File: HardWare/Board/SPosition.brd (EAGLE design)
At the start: 60 x 110 mm, 64 parts

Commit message: board and schem revisions
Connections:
- net GND: now also U$1.AGND
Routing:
- net GND: track 538.3 -> 561.0 mm, vias 0 -> 1
- net +3V3: track 77.2 -> 78.8 mm
- net OLEDCLK: track 60.2 -> 60.8 mm
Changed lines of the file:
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@@
 <wire x1="1.0922" y1="81.2740875" x2="1.0922" y2="96.5" width="0.1524" layer="16"/>
 <wire x1="2.9277" y1="58.0049875" x2="1.0922" y2="56.1694875" width="0.1524" layer="16"/>
-<wire x1="5.4716" y1="77.8946875" x2="3.3662875" y2="80" width="0.1524" layer="16"/>
+<wire x1="5.4716" y1="77.8946875" x2="3.8662875" y2="79.5" width="0.1524" layer="16"/>
+<wire x1="3.8662875" y1="79.5" x2="3.3662875" y2="80" width="0.1524" layer="16"/>
 <wire x1="2.3662875" y1="80" x2="1.0922" y2="81.2740875" width="0.1524" layer="16"/>
 <wire x1="2.9277" y1="71.4454125" x2="5.4716" y2="73.9893125" width="0.1524" layer="16"/>
@@
 <wire x1="51.278" y1="66.1596" x2="51.5" y2="65.9376" width="0.1524" layer="16"/>
 <wire x1="51.278" y1="66.1596" x2="51.056" y2="65.9376" width="0.1524" layer="16"/>
-<wire x1="11.235" y1="82.692" x2="11.235" y2="80" width="0.1524" layer="16"/>
-<wire x1="11.235" y1="80" x2="11.235" y2="79.5" width="0.1524" layer="16"/>
-<wire x1="11.235" y1="80" x2="3.3662875" y2="80" width="0.1524" layer="16"/>
+<wire x1="11.235" y1="82.692" x2="11.235" y2="79.5" width="0.1524" layer="16"/>
+<wire x1="11.235" y1="79.5" x2="3.8662875" y2="79.5" width="0.1524" layer="16"/>
 <wire x1="3.3662875" y1="80" x2="2.3662875" y2="80" width="0.1524" layer="16"/>
 <wire x1="48.0368" y1="65.9376" x2="47.0368" y2="65.9376" width="0.1524" layer="16"/>
@@
 <wire x1="21.995" y1="81.83" x2="22.325" y2="82.16" width="0.1524" layer="16"/>
 <wire x1="21.995" y1="81.83" x2="21.995" y2="79.5" width="0.1524" layer="16"/>
-<wire x1="11.235" y1="79.5" x2="21.995" y2="79.5" width="0.1524" layer="16"/>
+<wire x1="11.235" y1="79.5" x2="21" y2="79.5" width="0.1524" layer="16"/>
+<wire x1="20.5" y1="79.5" x2="21.995" y2="79.5" width="0.1524" layer="16"/>
 <wire x1="6.371" y1="11.125" x2="8.625" y2="11.125" width="0.1524" layer="16"/>
 <wire x1="8.625" y1="11.125" x2="9" y2="11.5" width="0.1524" layer="16"/>
@@
 <wire x1="52.5" y1="20.5" x2="47.34" y2="20.5" width="0.1524" layer="16"/>
 <wire x1="46" y1="19.16" x2="47.34" y2="20.5" width="0.1524" layer="16"/>
+<contactref element="U$1" pad="AGND"/>
+<wire x1="21.825" y1="81.66" x2="22.325" y2="82.16" width="0.1524" layer="1"/>
+<wire x1="21" y1="59.825" x2="21" y2="66.5" width="0.1524" layer="1"/>
+<wire x1="19.376" y1="58.201" x2="21" y2="59.825" width="0.1524" layer="1"/>
+<via x="21" y="66.5" extent="1-16" drill="0.35"/>
+<wire x1="21" y1="79.5" x2="21" y2="66.5" width="0.1524" layer="16"/>
 <wire x1="55.118" y1="96.505" x2="55.118" y2="96.5002" width="0" layer="19" extent="1-1"/>
 <wire x1="45.085" y1="96.5002" x2="45.085" y2="96.505" width="0" layer="19" extent="1-1"/>
@@
 <wire x1="20.7308" y1="29" x2="20.7308" y2="55.671" width="0.1524" layer="16"/>
 <wire x1="24.865" y1="81.66" x2="24.865" y2="82.16" width="0.1524" layer="1"/>
-<wire x1="24.865" y1="81.66" x2="22.3525" y2="79.1475" width="0.1524" layer="1"/>
-<wire x1="20.725" y1="55.661" x2="20.725" y2="64.86" width="0.1524" layer="1"/>
+<wire x1="24.865" y1="81.66" x2="23.3525" y2="80.1475" width="0.1524" layer="1"/>
+<wire x1="23.3525" y1="55.661" x2="23.3525" y2="80.1475" width="0.1524" layer="1"/>
 <wire x1="20.7308" y1="29" x2="13" y2="29" width="0.1524" layer="16"/>
 <contactref element="U$4" pad="VIN"/>
 <wire x1="9.452" y1="32.548" x2="2.576" y2="32.548" width="0.1524" layer="16"/>
 <wire x1="13" y1="29" x2="9.452" y2="32.548" width="0.1524" layer="16"/>
-<wire x1="20.725" y1="55.661" x2="19.376" y2="55.661" width="0.1524" layer="1"/>
-<wire x1="20.725" y1="64.86" x2="22.3525" y2="66.4875" width="0.1524" layer="1"/>
-<wire x1="22.3525" y1="66.4875" x2="22.3525" y2="79.1475" width="0.1524" layer="1"/>
+<wire x1="23.3525" y1="55.661" x2="19.376" y2="55.661" width="0.1524" layer="1"/>
 </signal>
 <signal name="ENC1SW">
@@
 <contactref element="U$1" pad="13/SCK"/>
 <contactref element="SSD1306-128X64" pad="3"/>
-<wire x1="19.376" y1="27.721" x2="23.5" y2="27.721" width="0.1524" layer="1"/>
-<wire x1="27.405" y1="82.16" x2="23.5" y2="78.255" width="0.1524" layer="1"/>
-<wire x1="23.5" y1="78.255" x2="23.5" y2="27.721" width="0.1524" layer="1"/>
+<wire x1="19.376" y1="27.721" x2="24.5" y2="27.721" width="0.1524" layer="1"/>
+<wire x1="27.405" y1="82.16" x2="24.5" y2="79.255" width="0.1524" layer="1"/>
+<wire x1="24.5" y1="79.255" x2="24.5" y2="27.721" width="0.1524" layer="1"/>
 </signal>
 <signal name="OLEDDATA">

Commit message: schematic and pcb rev4
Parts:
- added C1-10UF, C2-10UF: 10uF, rcl:C0805
- added C3-100N, C4-100N, C5-100N, C6-100N, C7-100N, C8-100N: 100n, rcl:C0805
- R1, R10, R11, R12, R13, R14, R15, R16, R17, R18, R19, R2, R20, R21, R22, R23, R24, R25, R26, R27, R28, R29, R3, R30, R31, R32, R33, R34, R35, R36, R4, R5, R6, R7, R8, R9: device Clean-Kong:R0805 -> rcl:R0805
- S1, S2: value (none) -> SW9mm
- moved D2 4.25 mm to (42.8, 3.50)
- moved D1 0.50 mm to (6.95, 22.2)
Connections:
- net +5V: now also C2-10UF.1, C3-100N.1, C4-100N.1
- net GND: now also C1-10UF.2, C2-10UF.2, C3-100N.2, C4-100N.2, C5-100N.2, C6-100N.2, C7-100N.2, C8-100N.2
- net VCC: now also C1-10UF.1, C5-100N.1, C6-100N.1
- net VSS: now also C7-100N.1, C8-100N.1
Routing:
- net GND: track 561.0 -> 610.9 mm
- net VSS: track 70.8 -> 86.6 mm
- net VCC: track 59.7 -> 75.2 mm
- net +5V: track 134.8 -> 148.8 mm
- net N$29: track 40.0 -> 35.7 mm
- net DAC2MOSI: track 27.1 -> 26.4 mm
- net DAC2CS: track 27.9 -> 27.2 mm

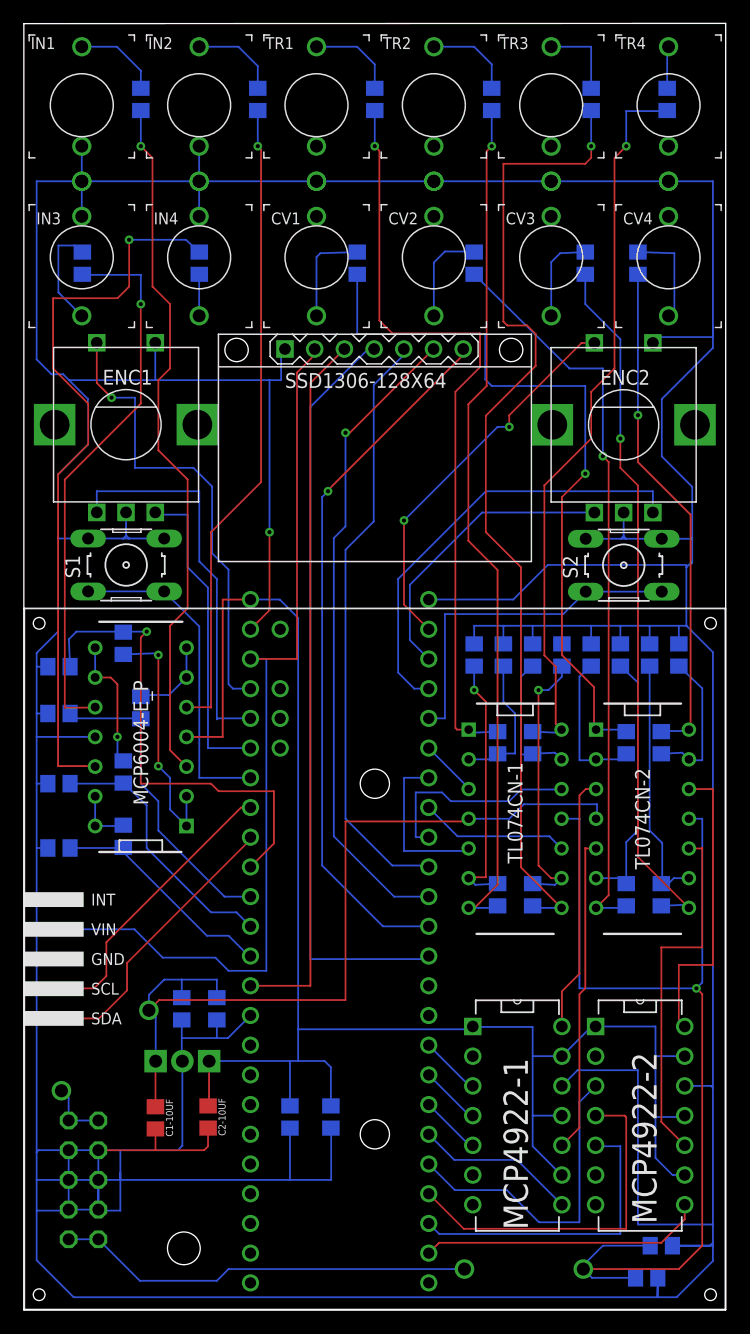
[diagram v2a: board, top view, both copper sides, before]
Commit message: noise reduction capacitors
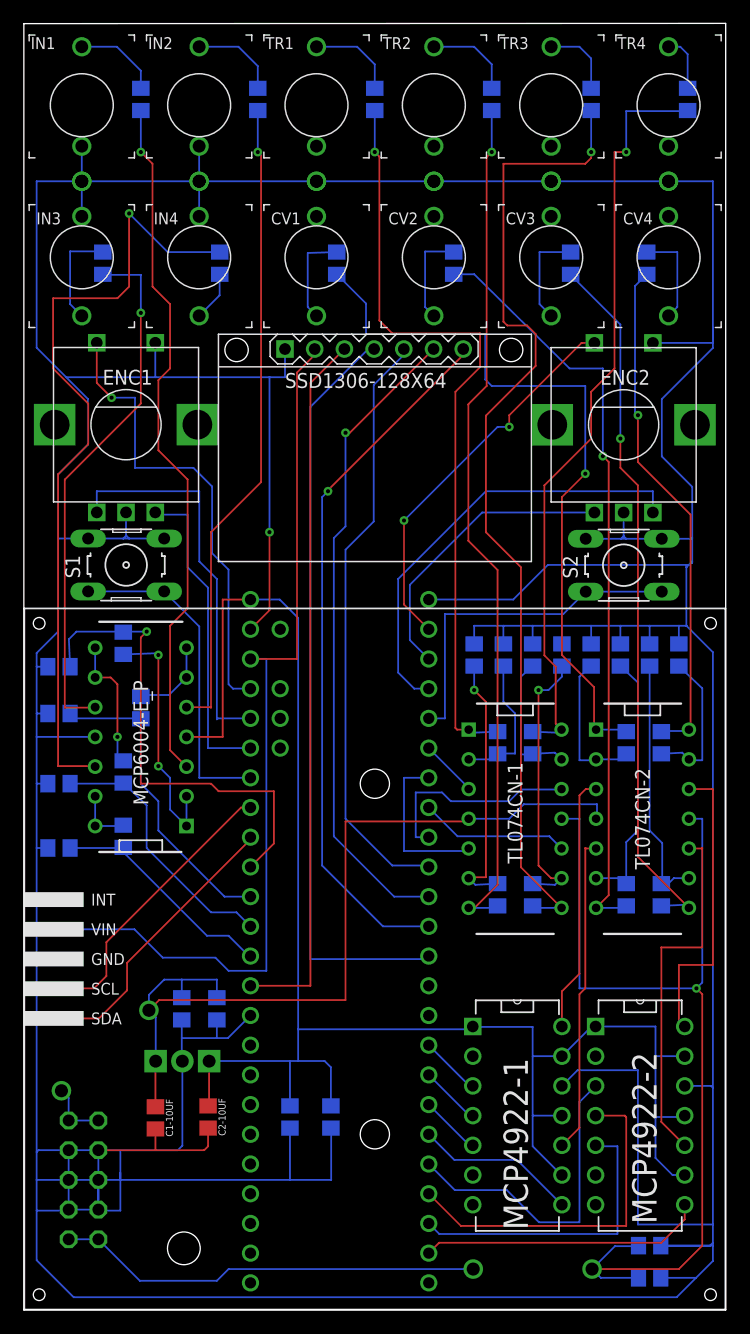
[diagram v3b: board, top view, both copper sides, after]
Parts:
- moved R15 1.75 mm to (56.8, 103.5)
- moved R18 1.75 mm to (36.8, 89.5)
- moved R24 1.75 mm to (26.8, 89.5)
- moved R3 1.75 mm to (6.75, 89.5)
- moved R4 1.75 mm to (16.8, 89.5)
- moved R21 1.25 mm to (46.8, 89.5)
- moved C8-100N 1.00 mm to (53.5, 5.50)
- moved D2 0.75 mm to (43.5, 3.50)
- moved R27 0.75 mm to (53.2, 89.5)
- moved C7-100N 0.25 mm to (53.5, 2.75)
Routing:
- net N$16: track 62.8 -> 67.8 mm
- net VSS: track 86.6 -> 83.4 mm
- net N$39: track 62.5 -> 64.8 mm
- net N$15: track 47.3 -> 45.6 mm
- net N$2: track 63.7 -> 65.5 mm
- net N$40: track 3.60 -> 4.82 mm
- net GND: track 610.9 -> 611.7 mm
- net N$29: track 35.7 -> 36.5 mm
- net N$20: track 7.82 -> 8.53 mm
- net N$9: track 3.72 -> 4.37 mm
- net N$36: track 6.97 -> 6.38 mm
- net N$27: track 43.6 -> 44.1 mm
- net N$21: track 60.3 -> 60.8 mm
- net DAC2MOSI: track 26.4 -> 25.9 mm

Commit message: updated pcb and schematic
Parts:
- moved D1 0.75 mm to (6.95, 22.9), turned to 306.8 degrees
- moved C5-100N 0.25 mm to (13.2, 25.8)
- moved C6-100N 0.25 mm to (16.2, 25.8)
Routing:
- net VCC: track 75.2 -> 76.8 mm
- net TRLSCL: track 24.9 -> 23.6 mm
- net TRLSDA: track 24.7 -> 23.5 mm

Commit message: pcb optimization
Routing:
- net N$39: track 64.8 -> 64.2 mm
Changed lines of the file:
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@@
 <wire x1="21.376" y1="39.881" x2="21.376" y2="44.35" width="0.1524" layer="1"/>
 <wire x1="19.376" y1="37.881" x2="21.376" y2="39.881" width="0.1524" layer="1"/>
-<wire x1="16" y1="45" x2="10" y2="45" width="0.1524" layer="1"/>
+<wire x1="15.75" y1="45.25" x2="10" y2="45.25" width="0.1524" layer="1"/>
 <wire x1="10" y1="57.5" x2="10.5" y2="58" width="0.1524" layer="1"/>
 <via x="10.5" y="58" extent="1-16" drill="0.35"/>
@@
 <wire x1="8.65" y1="58" x2="8.5" y2="57.95" width="0.1524" layer="16"/>
 <wire x1="21.376" y1="44.35" x2="16.65" y2="44.35" width="0.1524" layer="1"/>
-<wire x1="16.65" y1="44.35" x2="16" y2="45" width="0.1524" layer="1"/>
-<wire x1="10" y1="45" x2="10" y2="57.5" width="0.1524" layer="1"/>
+<wire x1="16.65" y1="44.35" x2="15.75" y2="45.25" width="0.1524" layer="1"/>
+<wire x1="10" y1="45.25" x2="10" y2="57.5" width="0.1524" layer="1"/>
 </signal>
 <signal name="CVIN2">
@@
 <wire x1="45.97" y1="34.38" x2="43.77" y2="34.38" width="0.1524" layer="16"/>
 <wire x1="43.77" y1="34.38" x2="43.5" y2="34.55" width="0.1524" layer="16"/>
-<wire x1="48.5" y1="102.55" x2="48.5" y2="99.25" width="0.1524" layer="16"/>
-<wire x1="48.5" y1="99.25" x2="48.25" y2="99" width="0.1524" layer="16"/>
-<via x="48.25" y="99" extent="1-16" drill="0.35"/>
-<wire x1="48.25" y1="99" x2="48.25" y2="98" width="0.1524" layer="1"/>
+<wire x1="48.5" y1="102.55" x2="48.5" y2="99" width="0.1524" layer="16"/>
+<via x="48.5" y="99" extent="1-16" drill="0.35"/>
+<wire x1="48.5" y1="99" x2="48.5" y2="98" width="0.1524" layer="1"/>
 <wire x1="42.5" y1="37.85" x2="45.97" y2="34.38" width="0.1524" layer="1"/>
 <wire x1="42.5" y1="63.5" x2="42.5" y2="37.85" width="0.1524" layer="1"/>
 <wire x1="43.7532" y1="80.71388125" x2="39.5" y2="76.46068125" width="0.1524" layer="1"/>
-<wire x1="41" y1="98" x2="48.25" y2="98" width="0.1524" layer="1"/>
+<wire x1="41" y1="98" x2="48.5" y2="98" width="0.1524" layer="1"/>
 <wire x1="41" y1="84.5" x2="41" y2="98" width="0.1524" layer="1"/>
 <wire x1="43.7532" y1="80.71388125" x2="43.7532" y2="83.44711875" width="0.1524" layer="1"/>
@@
 <wire x1="52" y1="102.5" x2="52" y2="99" width="0.1524" layer="16"/>
 <via x="52" y="99" extent="1-16" drill="0.35"/>
-<wire x1="50.5" y1="99" x2="52" y2="99" width="0.1524" layer="1"/>
 <wire x1="45.47" y1="50.12" x2="45.47" y2="55" width="0.1524" layer="1"/>
 <wire x1="45.97" y1="49.62" x2="45.47" y2="50.12" width="0.1524" layer="1"/>
-<wire x1="50.5" y1="80.5" x2="50.5" y2="99" width="0.1524" layer="1"/>
+<wire x1="50.5" y1="80.5" x2="50.5" y2="98" width="0.1524" layer="1"/>
 <wire x1="45.47" y1="55" x2="44.5" y2="55.97" width="0.1524" layer="1"/>
 <wire x1="44.5" y1="55.97" x2="44.5" y2="70.5" width="0.1524" layer="1"/>
@@
 <wire x1="48.5" y1="78.5" x2="50.5" y2="80.5" width="0.1524" layer="1"/>
 <wire x1="48.5" y1="74.5" x2="48.5" y2="78.5" width="0.1524" layer="1"/>
+<wire x1="50.5" y1="98" x2="51.5" y2="99" width="0.1524" layer="1"/>
+<wire x1="51.5" y1="99" x2="52" y2="99" width="0.1524" layer="1"/>
 </signal>
 <signal name="N$40">
@@
 <contactref element="MCP4922-1" pad="14"/>
 <contactref element="TL074CN-2" pad="3"/>
-<wire x1="47.5" y1="28.74" x2="46" y2="27.24" width="0.1524" layer="1"/>
+<wire x1="47.25" y1="28.49" x2="46" y2="27.24" width="0.1524" layer="1"/>
 <wire x1="46" y1="24.24" x2="46" y2="27.24" width="0.1524" layer="1"/>
-<wire x1="47.5" y1="28.74" x2="47.5" y2="44" width="0.1524" layer="1"/>
-<wire x1="47.5" y1="44" x2="48.04" y2="44.54" width="0.1524" layer="1"/>
+<wire x1="47.25" y1="28.49" x2="47.25" y2="43.75" width="0.1524" layer="1"/>
+<wire x1="47.25" y1="43.75" x2="48.04" y2="44.54" width="0.1524" layer="1"/>
 <wire x1="48.04" y1="44.54" x2="48.92" y2="44.54" width="0.1524" layer="1"/>
 </signal>

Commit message: pcb rev5
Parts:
- U$4: value SPREV3 -> SPREV5; device Adafruit Trellis:SPREV3 -> Adafruit Trellis:SPREV5
- moved MCP4922-1 0.50 mm to (46.0, 8.50)
- moved MCP4922-2 0.50 mm to (56.5, 8.50)
- moved C8-100N 0.35 mm to (53.2, 5.75)
- moved C5-100N 0.25 mm to (13.2, 25.5)
- moved C6-100N 0.25 mm to (16.2, 25.5)
- moved C7-100N 0.25 mm to (53.2, 2.75)
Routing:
- net GND: track 611.8 -> 603.7 mm
- net CV1: track 22.0 -> 29.3 mm
- net DAC2SCK: track 30.0 -> 28.4 mm
- net VCC: track 76.8 -> 76.0 mm
- net DAC2MOSI: track 25.9 -> 25.3 mm
- net CV4: track 30.9 -> 31.4 mm
- net CV3: track 25.4 -> 25.9 mm
- net CV2: track 27.2 -> 27.7 mm
